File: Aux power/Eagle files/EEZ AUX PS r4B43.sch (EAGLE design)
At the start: 58 parts, among them IC1 LM25575, IC2 MC7812, Q1 BTA26-600, Q2 BTA26-600, Q3 IRLL014N, X1 282836-5, X2 09185067324, X3 22-23-2031, X4 22-23-2031

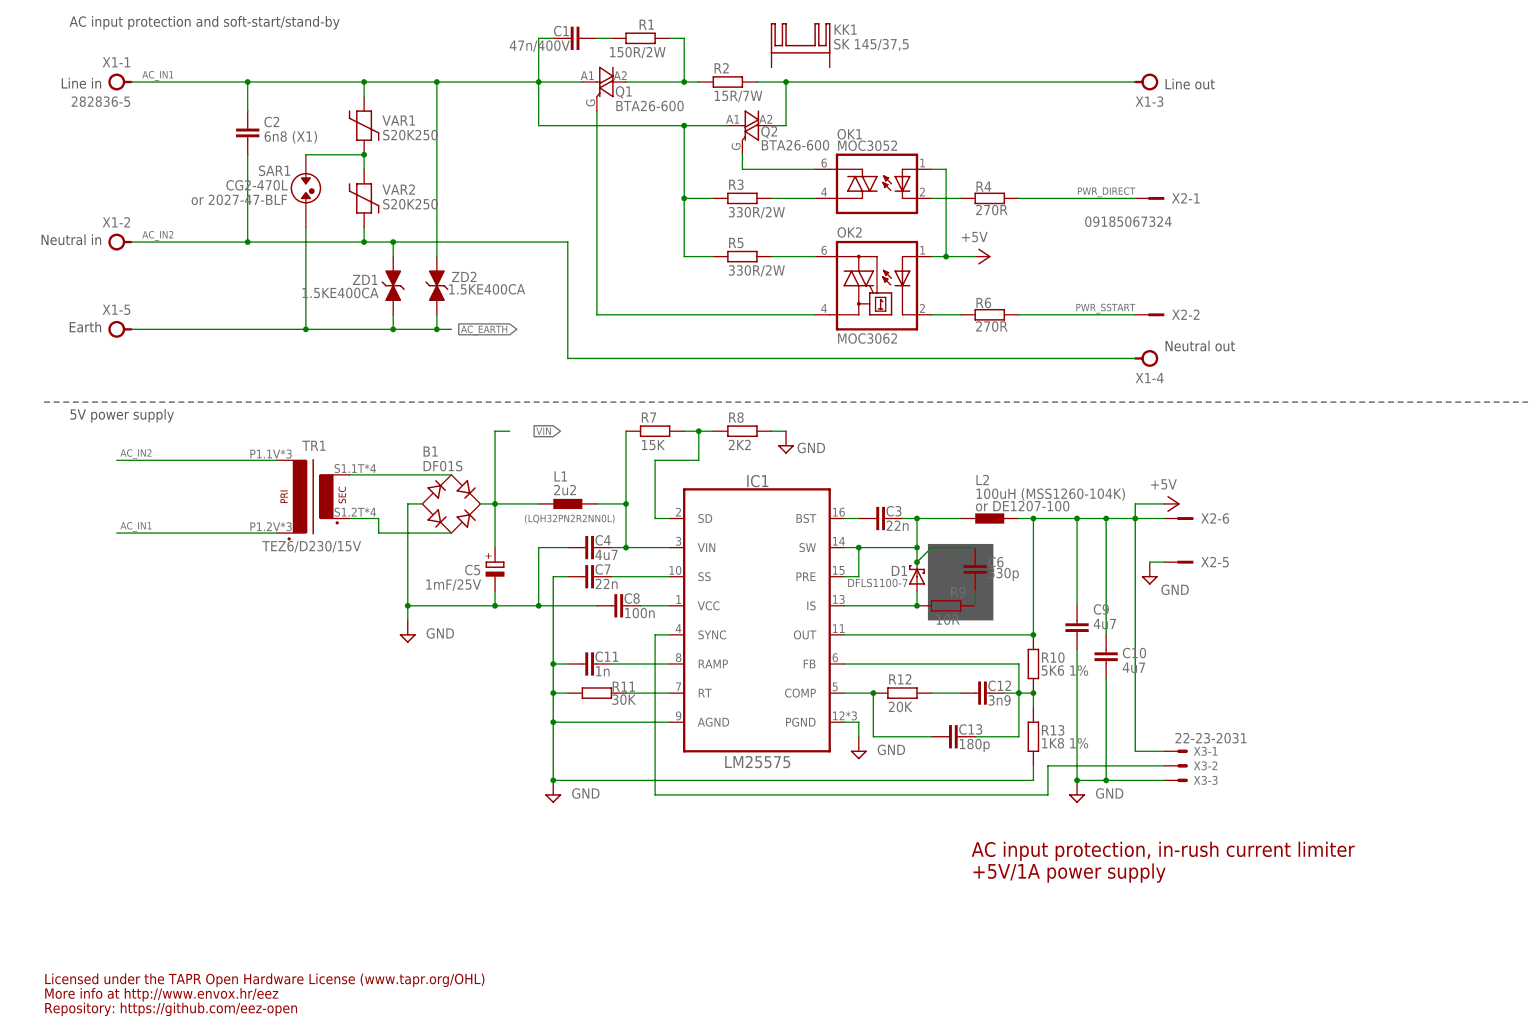
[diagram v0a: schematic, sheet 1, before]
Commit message: AUX PS r4B3, various BOM corrections
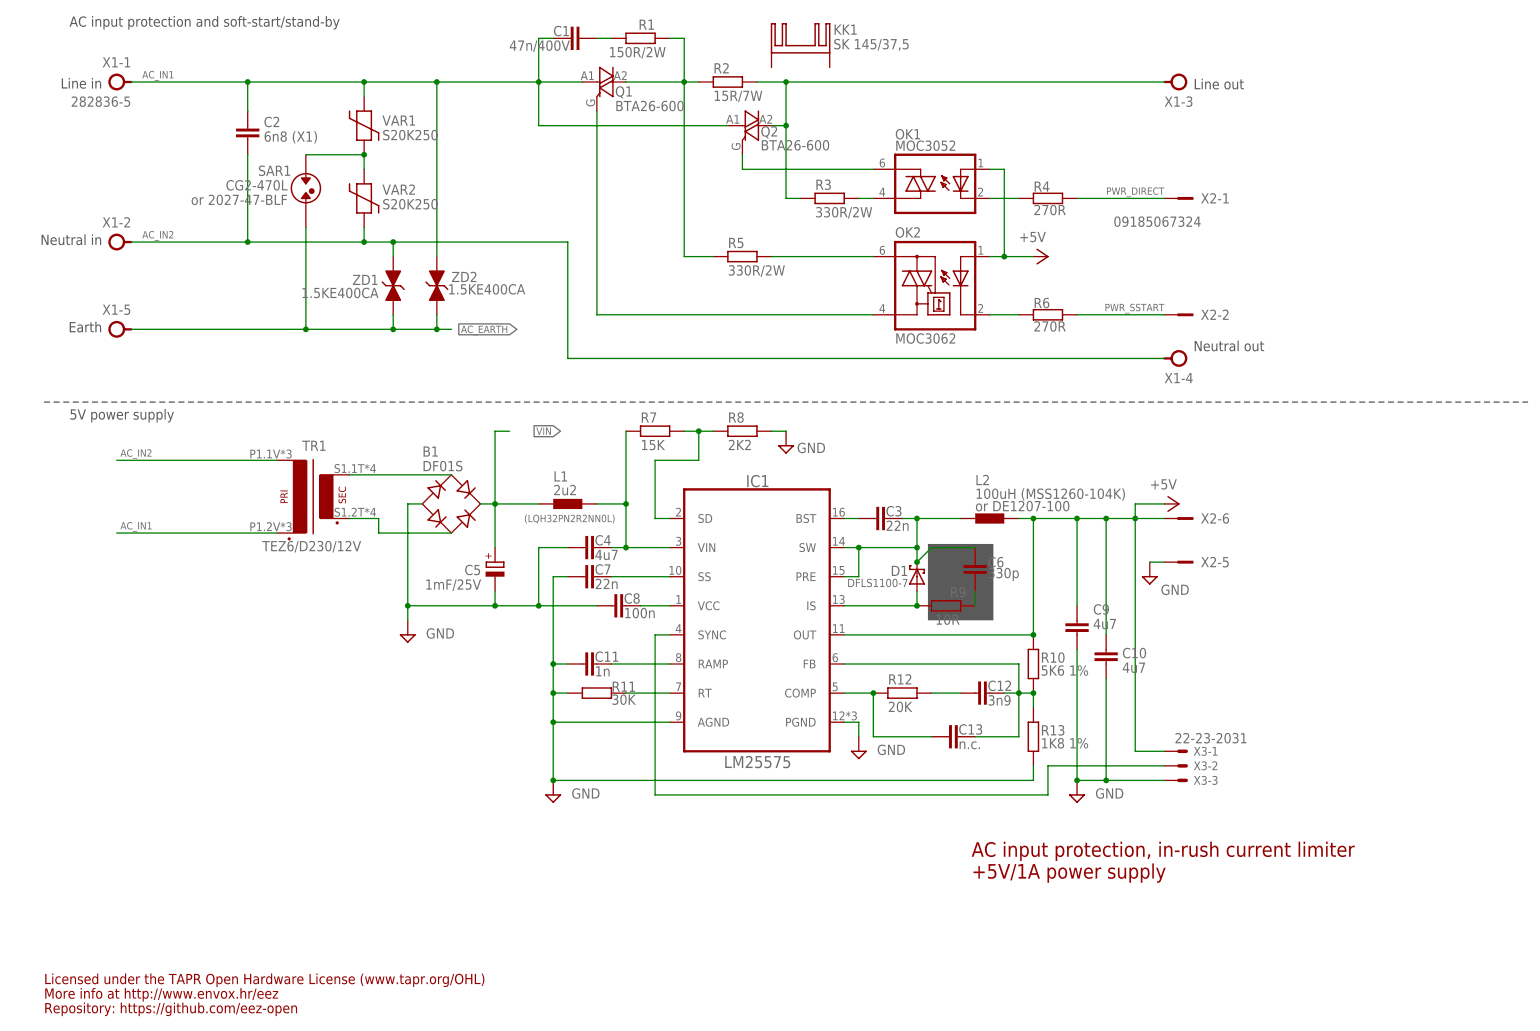
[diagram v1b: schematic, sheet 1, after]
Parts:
- C13: value 180p -> n.c.
- JP1: value (none) -> 826926-2
- TR1: value TEZ6/D230/15V -> TEZ6/D230/12V
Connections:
- removed net N$25: Q1.A2, R1.2, R2.1
- new net N$11: Q1.A2, R1.2, R2.1, R5.2
- net AC_IN1: no longer R3.2, R5.2
- net N$8: now also R3.2
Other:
- moved on the sheet: OK1, OK2, R3, R4, R6, X1-3, X1-4, X2-1, X2-2
